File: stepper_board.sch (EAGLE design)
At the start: 9 parts

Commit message: Removed TI DRV8825 from schematic and remove its library
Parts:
- removed U$2, U$3, U$4: DRV8825PWP, drv88xx:DRV8825PWP
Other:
- note removed: "8825 option"
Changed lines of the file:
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@@
 <?xml version="1.0" encoding="utf-8"?>
 <!DOCTYPE eagle SYSTEM "eagle.dtd">
-<eagle version="6.6.0">
+<eagle version="7.7.0">
 <drawing>
 <settings>
@@
 <parts>
 <part name="U$1" library="stm32f4" deviceset="STM32F4V_100PIN_GPSBOARD" device=""/>
-<part name="U$2" library="drv88xx" deviceset="DRV8825PWP" device=""/>
-<part name="U$3" library="drv88xx" deviceset="DRV8825PWP" device=""/>
-<part name="U$4" library="drv88xx" deviceset="DRV8825PWP" device=""/>
 <part name="Q1" library="special" deviceset="XTAL/S" device=""/>
 <part name="SUPPLY1" library="supply2" deviceset="GND" device=""/>
@@
 <sheet>
 <plain>
-<text x="88.9" y="91.44" size="1.778" layer="91">8825 option</text>
 <text x="91.44" y="15.24" size="1.778" layer="91">L6470 option</text>
 </plain>
 <instances>
 <instance part="U$1" gate="G$1" x="17.78" y="63.5"/>
-<instance part="U$2" gate="G$1" x="132.08" y="91.44"/>
-<instance part="U$3" gate="G$1" x="172.72" y="91.44"/>
-<instance part="U$4" gate="G$1" x="213.36" y="91.44"/>
 <instance part="Q1" gate="G$1" x="-58.42" y="111.76" rot="R180"/>
 <instance part="SUPPLY1" gate="GND" x="-58.42" y="99.06"/>

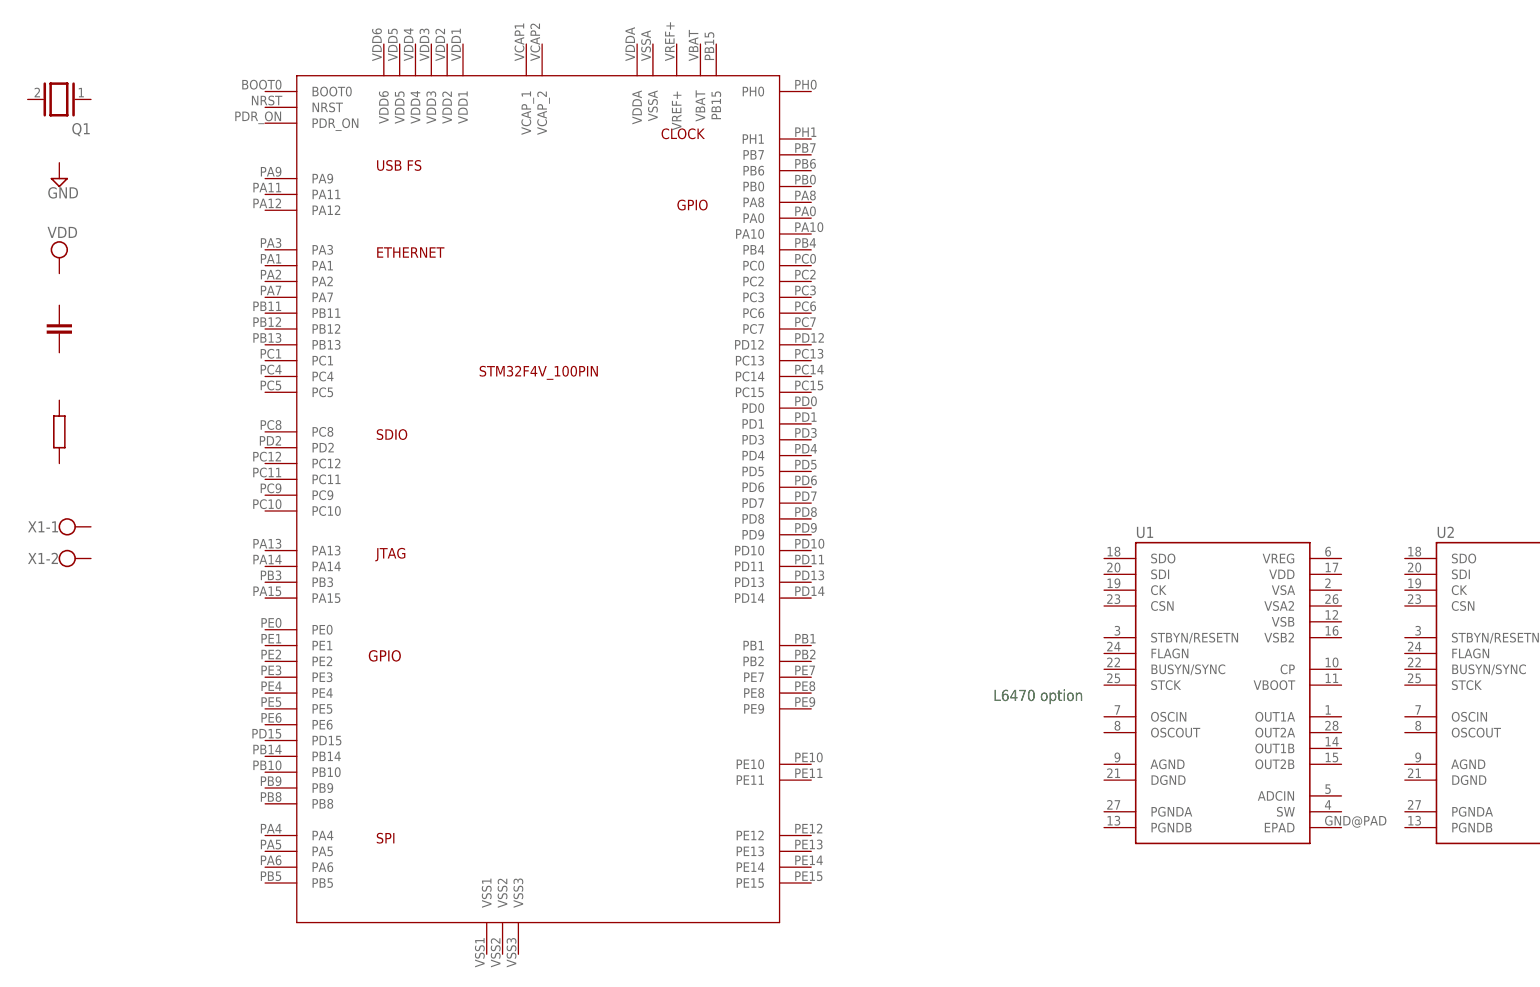
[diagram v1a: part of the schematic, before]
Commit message: Removed unnecessary library and added STM32F411RE to DigitalIC.lbr
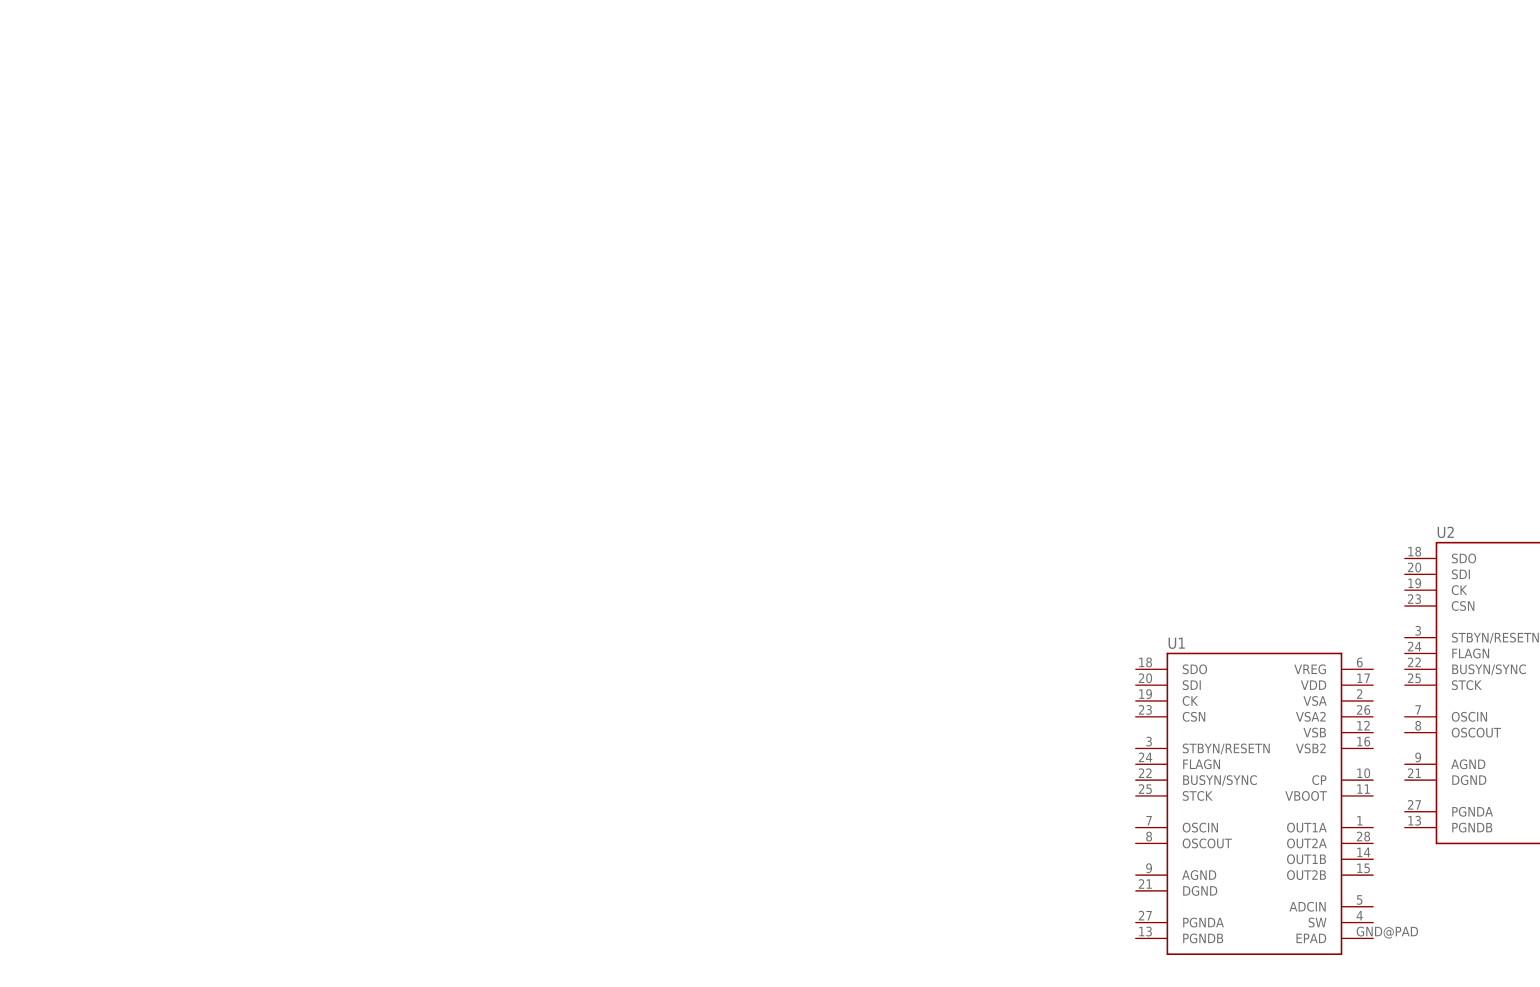
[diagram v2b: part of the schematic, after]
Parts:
- removed Q1: (no value), special:XTAL/S
- removed U$1: STM32F4V_100PIN_GPSBOARD, stm32f4:STM32F4V_100PIN_GPSBOARD
- removed X1: (no value), con-wago-500:W237-102
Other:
- note removed: "L6470 option"
- moved on the sheet: U1
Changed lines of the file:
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@@
 </classes>
 <parts>
-<part name="U$1" library="stm32f4" deviceset="STM32F4V_100PIN_GPSBOARD" device=""/>
-<part name="Q1" library="special" deviceset="XTAL/S" device=""/>
-<part name="SUPPLY1" library="supply2" deviceset="GND" device=""/>
-<part name="SUPPLY2" library="supply2" deviceset="VDD" device=""/>
-<part name="C1" library="docu-dummy" deviceset="C" device=""/>
-<part name="R1" library="docu-dummy" deviceset="R" device=""/>
 <part name="U1" library="SparkFun-PowerIC" deviceset="L6470" device=""/>
 <part name="U2" library="SparkFun-PowerIC" deviceset="L6470" device=""/>
 <part name="U3" library="SparkFun-PowerIC" deviceset="L6470" device=""/>
-<part name="X1" library="con-wago-500" deviceset="W237-102" device=""/>
 </parts>
 <sheets>
 <sheet>
 <plain>
-<text x="91.44" y="15.24" size="1.778" layer="91">L6470 option</text>
 </plain>
 <instances>
-<instance part="U$1" gate="G$1" x="17.78" y="63.5"/>
-<instance part="Q1" gate="G$1" x="-58.42" y="111.76" rot="R180"/>
-<instance part="SUPPLY1" gate="GND" x="-58.42" y="99.06"/>
-<instance part="SUPPLY2" gate="G$1" x="-58.42" y="86.36"/>
-<instance part="C1" gate="G$1" x="-58.42" y="76.2"/>
-<instance part="R1" gate="G$1" x="-58.42" y="58.42" rot="R90"/>
-<instance part="U1" gate="G$1" x="114.3" y="-7.62"/>
+<instance part="U1" gate="G$1" x="119.38" y="-25.4"/>
 <instance part="U2" gate="G$1" x="162.56" y="-7.62"/>
 <instance part="U3" gate="G$1" x="210.82" y="-7.62"/>
-<instance part="X1" gate="-1" x="-58.42" y="43.18"/>
-<instance part="X1" gate="-2" x="-58.42" y="38.1"/>
 </instances>
 <busses>

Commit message: Added correct MCU (STM32F411RE), started wiring MCU to drivers, and added datasheets
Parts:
- removed U1, U2, U3: (no value), SparkFun-PowerIC:L6470
- added L6470_1, L6470_2, L6470_3: (no value), SparkFun-PowerIC:L6470
- added STM32F411RE: STM32F411RE, DigitalIC:STM32F411RE
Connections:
- new net N$1: L6470_1.CK, L6470_2.CK, L6470_3.CK, STM32F411RE.PA5/SPI1_SCK
- new net N$2: L6470_1.SDI, L6470_2.SDI, L6470_3.SDI, STM32F411RE.PA7/SPI1_MOSI
- new net N$3: L6470_1.SDO, L6470_2.SDO, L6470_3.SDO, STM32F411RE.PA6/SPI1_MISO
- new net VCC: L6470_1.VSA, L6470_1.VSA2, L6470_1.VSB, L6470_1.VSB2, L6470_2.VSA, L6470_2.VSA2, L6470_2.VSB, L6470_2.VSB2, L6470_3.VSA, L6470_3.VSA2, L6470_3.VSB, L6470_3.VSB2
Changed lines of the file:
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@@
 </classes>
 <parts>
-<part name="U1" library="SparkFun-PowerIC" deviceset="L6470" device=""/>
-<part name="U2" library="SparkFun-PowerIC" deviceset="L6470" device=""/>
-<part name="U3" library="SparkFun-PowerIC" deviceset="L6470" device=""/>
+<part name="L6470_1" library="SparkFun-PowerIC" deviceset="L6470" device=""/>
+<part name="L6470_2" library="SparkFun-PowerIC" deviceset="L6470" device=""/>
+<part name="L6470_3" library="SparkFun-PowerIC" deviceset="L6470" device=""/>
+<part name="STM32F411RE" library="DigitalIC" deviceset="STM32F411RE" device=""/>
+<part name="VS" library="supply1" deviceset="VCC" device=""/>
+<part name="VS1" library="supply1" deviceset="VCC" device=""/>
+<part name="VS2" library="supply1" deviceset="VCC" device=""/>
 </parts>
 <sheets>
@@
 </plain>
 <instances>
-<instance part="U1" gate="G$1" x="119.38" y="-25.4"/>
-<instance part="U2" gate="G$1" x="162.56" y="-7.62"/>
-<instance part="U3" gate="G$1" x="210.82" y="-7.62"/>
+<instance part="L6470_1" gate="G$1" x="-96.52" y="30.48" rot="R180"/>
+<instance part="L6470_2" gate="G$1" x="-96.52" y="-22.86" rot="R180"/>
+<instance part="L6470_3" gate="G$1" x="-96.52" y="-76.2" rot="R180"/>
+<instance part="STM32F411RE" gate="STM32F411RE" x="0" y="0"/>
+<instance part="VS" gate="VCC" x="-142.24" y="2.54"/>
+<instance part="VS1" gate="VCC" x="-139.7" y="-50.8"/>
+<instance part="VS2" gate="VCC" x="-139.7" y="-104.14"/>
 </instances>
 <busses>
 </busses>
 <nets>
+<net name="N$1" class="0">
+<segment>
+<pinref part="L6470_1" gate="G$1" pin="CK"/>
+<pinref part="STM32F411RE" gate="STM32F411RE" pin="PA5/SPI1_SCK"/>
+<wire x1="-91.44" y1="-10.16" x2="-78.74" y2="-10.16" width="0.1524" layer="91"/>
+<pinref part="L6470_2" gate="G$1" pin="CK"/>
+<wire x1="-78.74" y1="-10.16" x2="-27.94" y2="-10.16" width="0.1524" layer="91"/>
+<wire x1="-91.44" y1="-63.5" x2="-78.74" y2="-63.5" width="0.1524" layer="91"/>
+<wire x1="-78.74" y1="-63.5" x2="-78.74" y2="-10.16" width="0.1524" layer="91"/>
+<junction x="-78.74" y="-10.16"/>
+<pinref part="L6470_3" gate="G$1" pin="CK"/>
+<wire x1="-78.74" y1="-63.5" x2="-78.74" y2="-116.84" width="0.1524" layer="91"/>
+<wire x1="-78.74" y1="-116.84" x2="-91.44" y2="-116.84" width="0.1524" layer="91"/>
+<junction x="-78.74" y="-63.5"/>
+</segment>
+</net>
+<net name="N$2" class="0">
+<segment>
+<pinref part="L6470_1" gate="G$1" pin="SDI"/>
+<wire x1="-91.44" y1="-12.7" x2="-76.2" y2="-12.7" width="0.1524" layer="91"/>
+<wire x1="-76.2" y1="-12.7" x2="-73.66" y2="-15.24" width="0.1524" layer="91"/>
+<pinref part="STM32F411RE" gate="STM32F411RE" pin="PA7/SPI1_MOSI"/>
+<wire x1="-73.66" y1="-15.24" x2="-71.12" y2="-15.24" width="0.1524" layer="91"/>
+<pinref part="L6470_2" gate="G$1" pin="SDI"/>
+<wire x1="-71.12" y1="-15.24" x2="-27.94" y2="-15.24" width="0.1524" layer="91"/>
+<wire x1="-71.12" y1="-15.24" x2="-71.12" y2="-66.04" width="0.1524" layer="91"/>
+<wire x1="-71.12" y1="-66.04" x2="-91.44" y2="-66.04" width="0.1524" layer="91"/>
+<junction x="-71.12" y="-15.24"/>
+<pinref part="L6470_3" gate="G$1" pin="SDI"/>
+<wire x1="-71.12" y1="-66.04" x2="-71.12" y2="-119.38" width="0.1524" layer="91"/>
+<wire x1="-71.12" y1="-119.38" x2="-91.44" y2="-119.38" width="0.1524" layer="91"/>
+<junction x="-71.12" y="-66.04"/>
+</segment>
+</net>
+<net name="N$3" class="0">
+<segment>
+<pinref part="STM32F411RE" gate="STM32F411RE" pin="PA6/SPI1_MISO"/>
+<wire x1="-27.94" y1="-12.7" x2="-68.58" y2="-12.7" width="0.1524" layer="91"/>
+<wire x1="-68.58" y1="-12.7" x2="-73.66" y2="-12.7" width="0.1524" layer="91"/>
+<wire x1="-73.66" y1="-12.7" x2="-76.2" y2="-15.24" width="0.1524" layer="91"/>
+<pinref part="L6470_1" gate="G$1" pin="SDO"/>
+<wire x1="-76.2" y1="-15.24" x2="-91.44" y2="-15.24" width="0.1524" layer="91"/>
+<pinref part="L6470_2" gate="G$1" pin="SDO"/>
+<wire x1="-68.58" y1="-12.7" x2="-68.58" y2="-68.58" width="0.1524" layer="91"/>
+<wire x1="-68.58" y1="-68.58" x2="-91.44" y2="-68.58" width="0.1524" layer="91"/>
+<junction x="-68.58" y="-12.7"/>
+<pinref part="L6470_3" gate="G$1" pin="SDO"/>
+<wire x1="-68.58" y1="-68.58" x2="-68.58" y2="-121.92" width="0.1524" layer="91"/>
+<wire x1="-68.58" y1="-121.92" x2="-91.44" y2="-121.92" width="0.1524" layer="91"/>
+<junction x="-68.58" y="-68.58"/>
+</segment>
+</net>
+<net name="VCC" class="0">
+<segment>
+<pinref part="L6470_1" gate="G$1" pin="VSB2"/>
+<wire x1="-129.54" y1="-2.54" x2="-134.62" y2="-2.54" width="0.1524" layer="91"/>
+<pinref part="L6470_1" gate="G$1" pin="VSB"/>
+<wire x1="-129.54" y1="-5.08" x2="-134.62" y2="-5.08" width="0.1524" layer="91"/>
+<wire x1="-134.62" y1="-5.08" x2="-134.62" y2="-2.54" width="0.1524" layer="91"/>
+<pinref part="L6470_1" gate="G$1" pin="VSA2"/>
+<wire x1="-129.54" y1="-7.62" x2="-134.62" y2="-7.62" width="0.1524" layer="91"/>
+<wire x1="-134.62" y1="-7.62" x2="-134.62" y2="-5.08" width="0.1524" layer="91"/>
+<junction x="-134.62" y="-5.08"/>
+<pinref part="L6470_1" gate="G$1" pin="VSA"/>
+<wire x1="-129.54" y1="-10.16" x2="-134.62" y2="-10.16" width="0.1524" layer="91"/>
+<wire x1="-134.62" y1="-10.16" x2="-134.62" y2="-7.62" width="0.1524" layer="91"/>
+<junction x="-134.62" y="-7.62"/>
+<pinref part="VS" gate="VCC" pin="VCC"/>
+<wire x1="-134.62" y1="-2.54" x2="-142.24" y2="-2.54" width="0.1524" layer="91"/>
+<wire x1="-142.24" y1="-2.54" x2="-142.24" y2="0" width="0.1524" layer="91"/>
+<junction x="-134.62" y="-2.54"/>
+</segment>
+<segment>
+<pinref part="L6470_2" gate="G$1" pin="VSB2"/>
+<pinref part="VS1" gate="VCC" pin="VCC"/>
+<wire x1="-129.54" y1="-55.88" x2="-134.62" y2="-55.88" width="0.1524" layer="91"/>
+<wire x1="-134.62" y1="-55.88" x2="-139.7" y2="-55.88" width="0.1524" layer="91"/>
+<wire x1="-139.7" y1="-55.88" x2="-139.7" y2="-53.34" width="0.1524" layer="91"/>
+<pinref part="L6470_2" gate="G$1" pin="VSB"/>
+<wire x1="-129.54" y1="-58.42" x2="-134.62" y2="-58.42" width="0.1524" layer="91"/>
+<wire x1="-134.62" y1="-58.42" x2="-134.62" y2="-55.88" width="0.1524" layer="91"/>
+<junction x="-134.62" y="-55.88"/>
+<pinref part="L6470_2" gate="G$1" pin="VSA2"/>
+<wire x1="-129.54" y1="-60.96" x2="-134.62" y2="-60.96" width="0.1524" layer="91"/>
+<wire x1="-134.62" y1="-60.96" x2="-134.62" y2="-58.42" width="0.1524" layer="91"/>
+<junction x="-134.62" y="-58.42"/>
+<pinref part="L6470_2" gate="G$1" pin="VSA"/>
+<wire x1="-129.54" y1="-63.5" x2="-134.62" y2="-63.5" width="0.1524" layer="91"/>
+<wire x1="-134.62" y1="-63.5" x2="-134.62" y2="-60.96" width="0.1524" layer="91"/>
+<junction x="-134.62" y="-60.96"/>
+</segment>
+<segment>
+<pinref part="L6470_3" gate="G$1" pin="VSB2"/>
+<pinref part="VS2" gate="VCC" pin="VCC"/>
+<wire x1="-129.54" y1="-109.22" x2="-134.62" y2="-109.22" width="0.1524" layer="91"/>
+<wire x1="-134.62" y1="-109.22" x2="-139.7" y2="-109.22" width="0.1524" layer="91"/>
+<wire x1="-139.7" y1="-109.22" x2="-139.7" y2="-106.68" width="0.1524" layer="91"/>
+<pinref part="L6470_3" gate="G$1" pin="VSB"/>
+<wire x1="-129.54" y1="-111.76" x2="-134.62" y2="-111.76" width="0.1524" layer="91"/>
+<wire x1="-134.62" y1="-111.76" x2="-134.62" y2="-109.22" width="0.1524" layer="91"/>
+<junction x="-134.62" y="-109.22"/>
+<pinref part="L6470_3" gate="G$1" pin="VSA2"/>
+<wire x1="-129.54" y1="-114.3" x2="-134.62" y2="-114.3" width="0.1524" layer="91"/>
+<wire x1="-134.62" y1="-114.3" x2="-134.62" y2="-111.76" width="0.1524" layer="91"/>
+<junction x="-134.62" y="-111.76"/>
+<pinref part="L6470_3" gate="G$1" pin="VSA"/>
+<wire x1="-129.54" y1="-116.84" x2="-134.62" y2="-116.84" width="0.1524" layer="91"/>
+<wire x1="-134.62" y1="-116.84" x2="-134.62" y2="-114.3" width="0.1524" layer="91"/>
+<junction x="-134.62" y="-114.3"/>
+</segment>
+</net>
 </nets>
 </sheet>

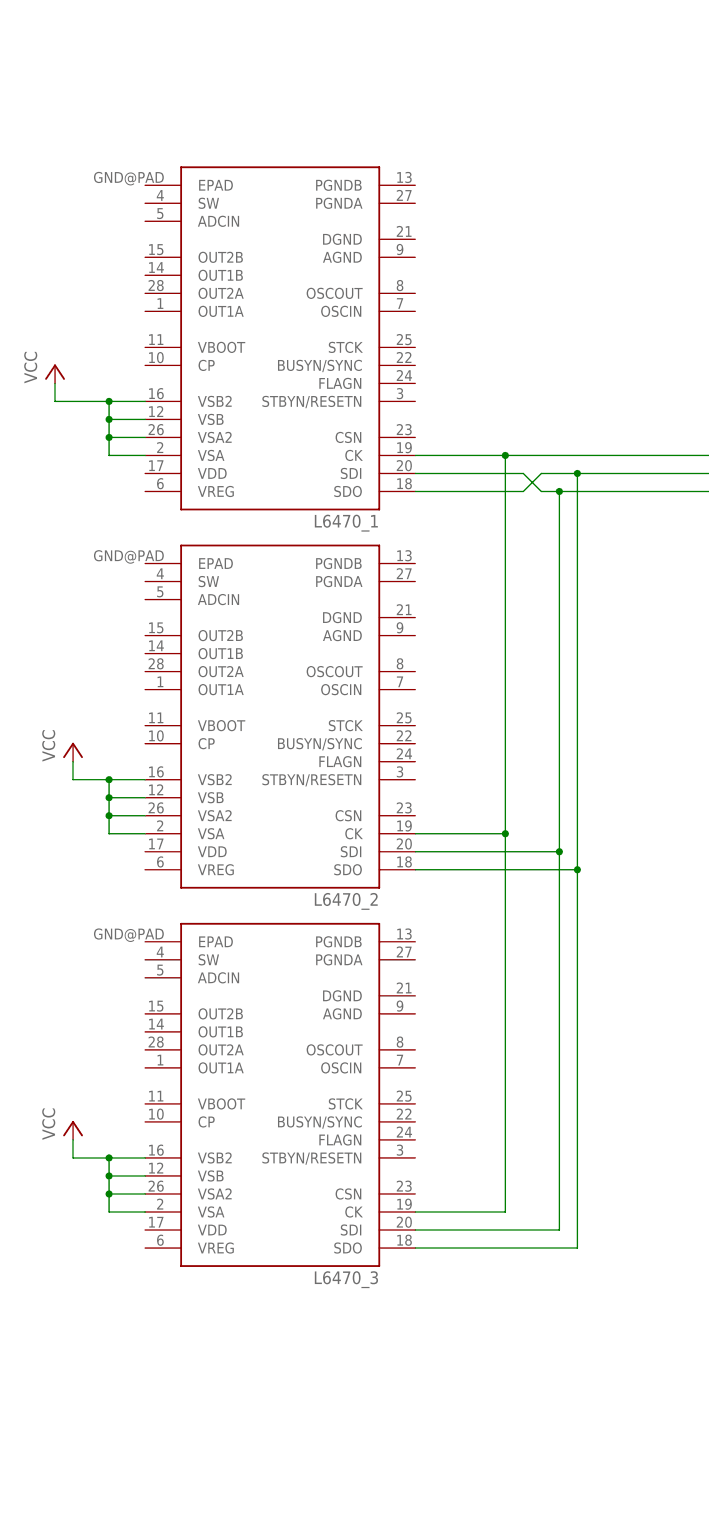
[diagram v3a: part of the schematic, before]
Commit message: Added some grounding connections to the driver chips on schematic
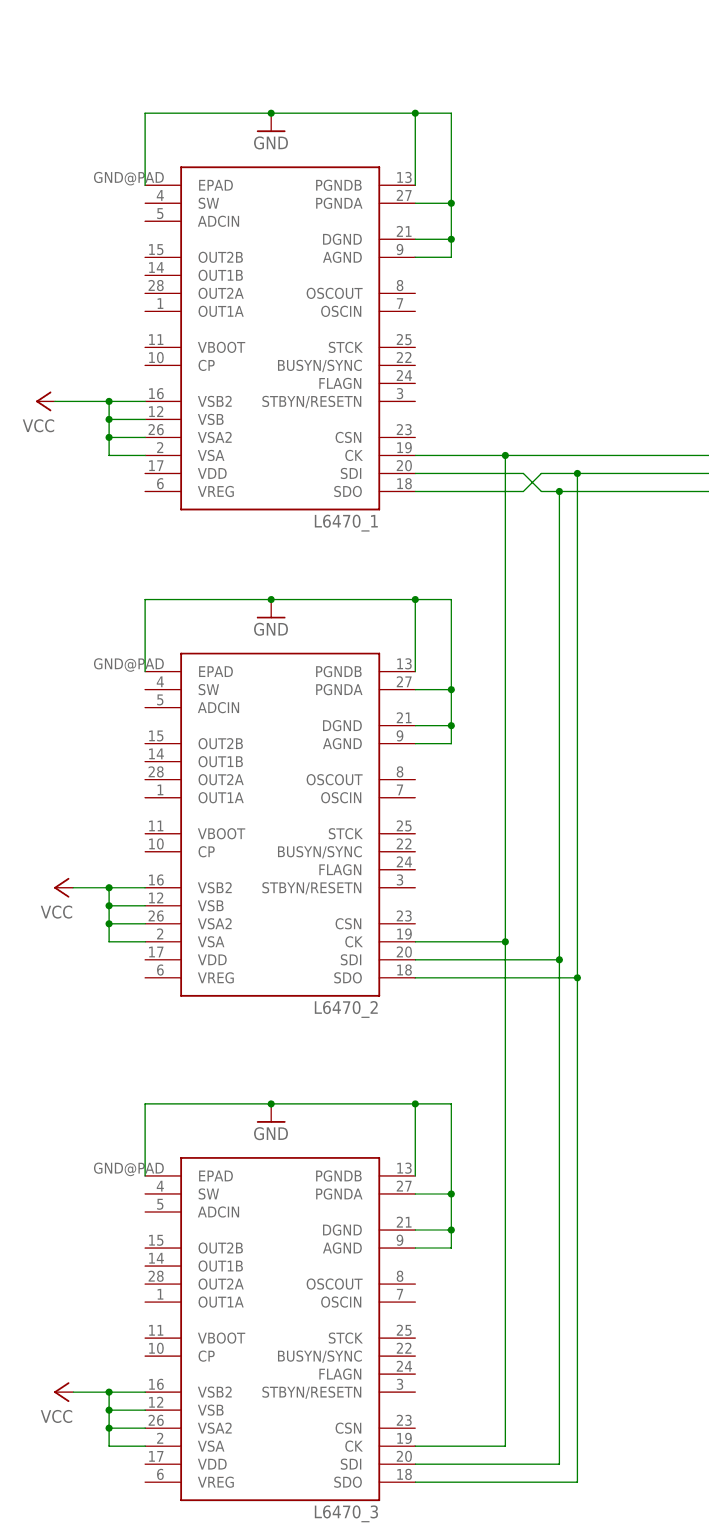
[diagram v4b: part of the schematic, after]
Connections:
- new net GND: L6470_1.AGND, L6470_1.DGND, L6470_1.EPAD, L6470_1.PGNDA, L6470_1.PGNDB, L6470_2.AGND, L6470_2.DGND, L6470_2.EPAD, L6470_2.PGNDA, L6470_2.PGNDB, L6470_3.AGND, L6470_3.DGND, L6470_3.EPAD, L6470_3.PGNDA, L6470_3.PGNDB
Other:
- moved on the sheet: L6470_2, L6470_3
